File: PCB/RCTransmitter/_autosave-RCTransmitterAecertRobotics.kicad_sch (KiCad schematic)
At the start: 41 parts, among them K1 KCD1 Power Switch

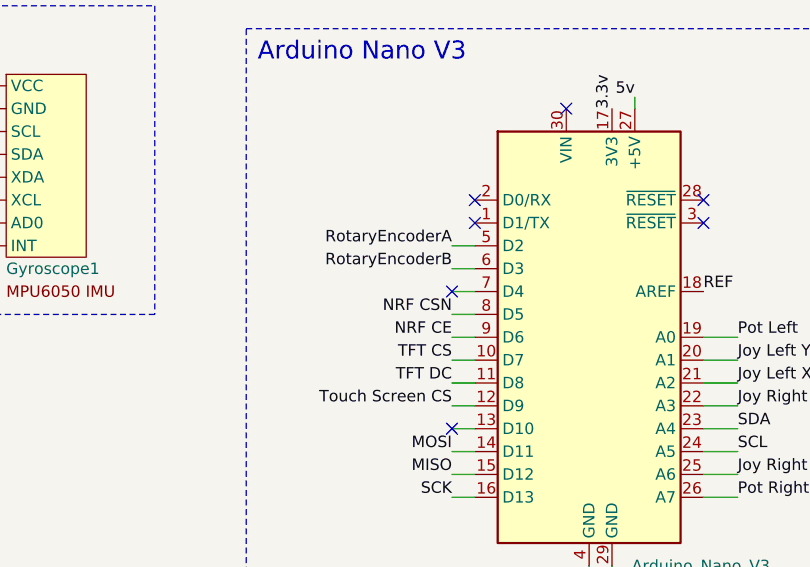
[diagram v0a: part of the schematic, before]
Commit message: nrf and screen not working at the same time
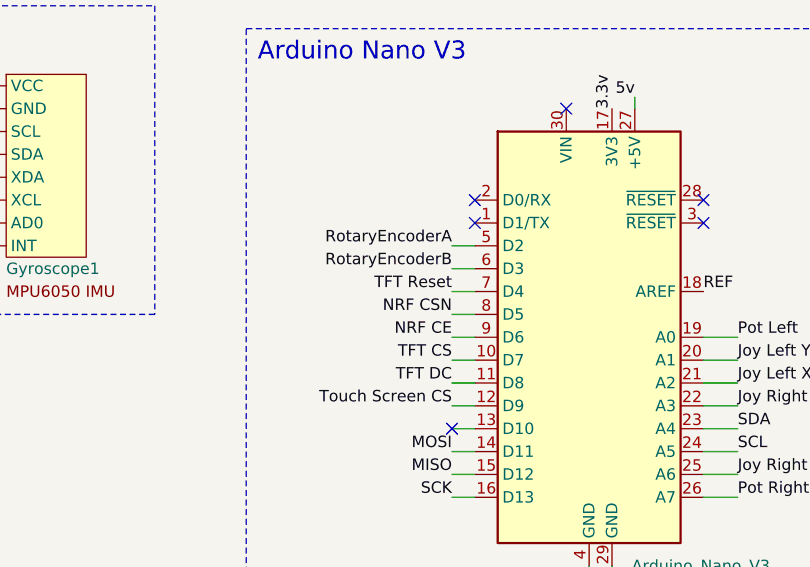
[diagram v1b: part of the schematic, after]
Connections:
- net TFT Reset: now also Arduino_Nano_V3.7 (D4)
- no-connect marks 23 -> 22
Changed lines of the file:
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@@
   (no_connect (at 175.26 120.65))
   (no_connect (at 175.26 118.11))
-  (no_connect (at 231.14 46.99))
   (no_connect (at 179.07 36.83))
   (no_connect (at 231.14 62.23))
@@
     (effects (font (size 1.27 1.27)) (justify right bottom))
   )
+  (label "TFT Reset" (at 231.14 46.99 180) (fields_autoplaced)
+    (effects (font (size 1.27 1.27)) (justify right bottom))
+  )
